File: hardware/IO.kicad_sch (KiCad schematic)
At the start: 34 parts, among them J1 Conn_01x04, J2 Screw_Terminal_01x06, J3 Screw_Terminal_01x02, J4 Screw_Terminal_01x04, J5 Conn_02x03_Odd_Even, J6 Conn_01x07, Q5 RE1C002UNTCL, Q6 RE1C002UNTCL, Q7 RE1C002UNTCL, Q8 RE1C002UNTCL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

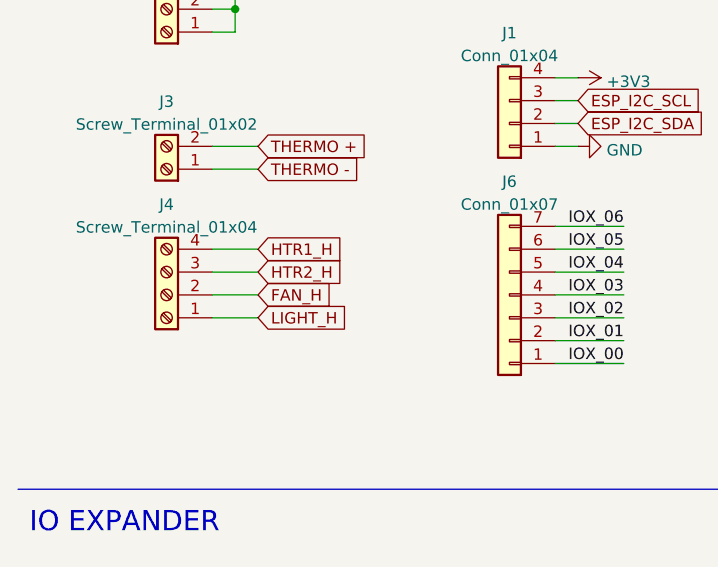
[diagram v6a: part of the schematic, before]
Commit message: major hardware refctoring to use modern parts that are still being made
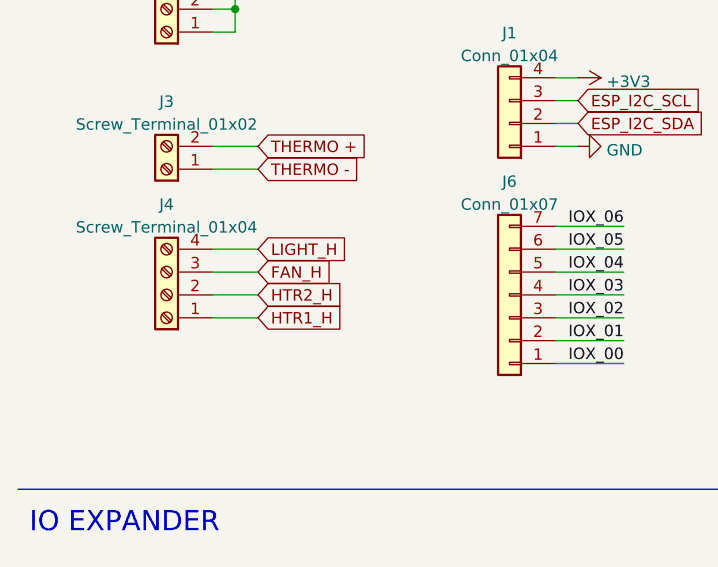
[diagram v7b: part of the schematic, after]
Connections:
- net FAN_H: now also J4.3 (Pin_3); no longer J4.2 (Pin_2)
- net HTR1_H: now also J4.1 (Pin_1); no longer J4.4 (Pin_4)
- net HTR2_H: now also J4.2 (Pin_2); no longer J4.3 (Pin_3)
- net LIGHT_H: now also J4.4 (Pin_4); no longer J4.1 (Pin_1)
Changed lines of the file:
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@@
     )
   )
-  (global_label "HTR2_H" (shape input) (at 38.1 69.85 0) (fields_autoplaced)
+  (global_label "HTR2_H" (shape input) (at 38.1 72.39 0) (fields_autoplaced)
     (effects (font (size 1.27 1.27)) (justify left))
-    (property "Intersheet References" "${INTERSHEET_REFS}" (id 0) (at 47.5888 69.7706 0)
+    (property "Intersheet References" "${INTERSHEET_REFS}" (id 0) (at 47.5888 72.3106 0)
       (effects (font (size 1.27 1.27)) (justify left) hide)
     )
   )
-  (global_label "LIGHT_H" (shape input) (at 38.1 74.93 0) (fields_autoplaced)
+  (global_label "LIGHT_H" (shape input) (at 38.1 67.31 0) (fields_autoplaced)
     (effects (font (size 1.27 1.27)) (justify left))
-    (property "Intersheet References" "${INTERSHEET_REFS}" (id 0) (at 46.3188 74.8506 0)
+    (property "Intersheet References" "${INTERSHEET_REFS}" (id 0) (at 46.3188 67.2306 0)
       (effects (font (size 1.27 1.27)) (justify left) hide)
     )
@@
     )
   )
-  (global_label "FAN_H" (shape input) (at 38.1 72.39 0) (fields_autoplaced)
+  (global_label "FAN_H" (shape input) (at 38.1 69.85 0) (fields_autoplaced)
     (effects (font (size 1.27 1.27)) (justify left))
-    (property "Intersheet References" "${INTERSHEET_REFS}" (id 0) (at 47.5888 72.3106 0)
+    (property "Intersheet References" "${INTERSHEET_REFS}" (id 0) (at 47.5888 69.7706 0)
       (effects (font (size 1.27 1.27)) (justify left) hide)
     )
@@
     )
   )
-  (global_label "HTR1_H" (shape input) (at 38.1 67.31 0) (fields_autoplaced)
+  (global_label "HTR1_H" (shape input) (at 38.1 74.93 0) (fields_autoplaced)
     (effects (font (size 1.27 1.27)) (justify left))
-    (property "Intersheet References" "${INTERSHEET_REFS}" (id 0) (at 47.5888 67.2306 0)
+    (property "Intersheet References" "${INTERSHEET_REFS}" (id 0) (at 47.5888 74.8506 0)
       (effects (font (size 1.27 1.27)) (justify left) hide)
     )
